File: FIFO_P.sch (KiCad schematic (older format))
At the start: 48 parts, among them J1 Vin, J3 ICLK, J4 Vout, SW1 Rotary_Encoder_61C, U1 SN74LVC2G157_MUX_TI, U10 AD7840, U2 IDT_ICS551, U3 LTC1740, U4 ARDUINO_DUE_FIFO_P_COMMANDS, U5 IDT_72V2105, U6 SN74LVC2G157_MUX_TI

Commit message: Updated missing footprints on schematic
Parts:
- C24, C32, C33, C34, C35: footprint (none) -> Capacitor_THT:C_Rect_L4.0mm_W2.5mm_P2.50mm
- NT1: footprint (none) -> NetTie:NetTie-2_SMD_Pad2.0mm
- U1, U6: footprint (none) -> Package_SO:SSOP-8_2.95x2.8mm_P0.65mm
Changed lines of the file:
@@
 F 0 "C32" H 10192 4896 50  0000 L CNN
 F 1 "0u1" H 10192 4805 50  0000 L CNN
-F 2 "" H 10100 4850 50  0001 C CNN
+F 2 "Capacitor_THT:C_Rect_L4.0mm_W2.5mm_P2.50mm" H 10100 4850 50  0001 C CNN
 F 3 "~" H 10100 4850 50  0001 C CNN
 	1    10100 4850
@@
 F 0 "C33" H 10192 5096 50  0000 L CNN
 F 1 "0u1" H 10192 5005 50  0000 L CNN
-F 2 "" H 10100 5050 50  0001 C CNN
+F 2 "Capacitor_THT:C_Rect_L4.0mm_W2.5mm_P2.50mm" H 10100 5050 50  0001 C CNN
 F 3 "~" H 10100 5050 50  0001 C CNN
 	1    10100 5050
@@
 F 0 "C34" H 10492 4896 50  0000 L CNN
 F 1 "1u" H 10492 4805 50  0000 L CNN
-F 2 "" H 10400 4850 50  0001 C CNN
+F 2 "Capacitor_THT:C_Rect_L4.0mm_W2.5mm_P2.50mm" H 10400 4850 50  0001 C CNN
 F 3 "~" H 10400 4850 50  0001 C CNN
 	1    10400 4850
@@
 F 0 "C35" H 10492 5096 50  0000 L CNN
 F 1 "1u" H 10492 5005 50  0000 L CNN
-F 2 "" H 10400 5050 50  0001 C CNN
+F 2 "Capacitor_THT:C_Rect_L4.0mm_W2.5mm_P2.50mm" H 10400 5050 50  0001 C CNN
 F 3 "~" H 10400 5050 50  0001 C CNN
 	1    10400 5050
@@
 F 0 "C24" H 10192 4546 50  0000 L CNN
 F 1 "0u1" H 10192 4455 50  0000 L CNN
-F 2 "" H 10100 4500 50  0001 C CNN
+F 2 "Capacitor_THT:C_Rect_L4.0mm_W2.5mm_P2.50mm" H 10100 4500 50  0001 C CNN
 F 3 "~" H 10100 4500 50  0001 C CNN
 	1    10100 4500
@@
 F 0 "U1" H 1800 2447 60  0000 C CNN
 F 1 "SN74LVC2G157_MUX_TI" H 1800 2341 60  0000 C CNN
-F 2 "" H 1800 1750 60  0000 C CNN
+F 2 "Package_SO:SSOP-8_2.95x2.8mm_P0.65mm" H 1800 1750 60  0001 C CNN
 F 3 "" H 1800 1750 60  0000 C CNN
 	1    1800 2050
@@
 Wire Wire Line
 	1350 2200 1350 2250
-$Comp
-L FIFO_P:SN74LVC2G157_MUX_TI U6
-U 1 1 5DD36A43
-P 1800 2850
-F 0 "U6" H 1800 3247 60  0000 C CNN
-F 1 "SN74LVC2G157_MUX_TI" H 1800 3141 60  0000 C CNN
-F 2 "" H 1800 2550 60  0000 C CNN
-F 3 "" H 1800 2550 60  0000 C CNN
-	1    1800 2850
-	1    0    0    -1
-$EndComp
 $Comp
 L power:GND #PWR06
@@
 F 0 "NT1" H 6700 7631 50  0000 C CNN
 F 1 "Net-Tie_2" H 6700 7540 50  0000 C CNN
-F 2 "" H 6700 7450 50  0001 C CNN
+F 2 "NetTie:NetTie-2_SMD_Pad2.0mm" H 6700 7450 50  0001 C CNN
 F 3 "~" H 6700 7450 50  0001 C CNN
 	1    6700 7450
@@
 Text GLabel 4350 1600 0    60   Input ~ 0
 CLK_EN
+Text GLabel 4350 2250 0    60   Input ~ 0
+DAC0
 Wire Bus Line
 	6650 6200 7550 6200
@@
 Wire Bus Line
 	7550 4150 7550 6200
-Text GLabel 4350 2250 0    60   Input ~ 0
-DAC0
+$Comp
+L FIFO_P:SN74LVC2G157_MUX_TI U6
+U 1 1 5DD36A43
+P 1800 2850
+F 0 "U6" H 1800 3247 60  0000 C CNN
+F 1 "SN74LVC2G157_MUX_TI" H 1800 3141 60  0000 C CNN
+F 2 "Package_SO:SSOP-8_2.95x2.8mm_P0.65mm" H 1800 2550 60  0001 C CNN
+F 3 "" H 1800 2550 60  0000 C CNN
+	1    1800 2850
+	1    0    0    -1
+$EndComp
 $EndSCHEMATC

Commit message: More schematic cleanup: reannotate and re-do footprints
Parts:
- removed U1, U6: SN74LVC2G157_MUX_TI, Package_SO:SSOP-8_2.95x2.8mm_P0.65mm, symbol FIFO_P:SN74LVC2G157_MUX_TI
- removed U10: AD7840, Package_DIP:DIP-24_W7.62mm, symbol FIFO_P:AD7840
- removed U2: IDT_ICS551, Package_SO:SOIC-8_3.9x4.9mm_P1.27mm, symbol FIFO_P:IDT_ICS551
- removed U3: LTC1740, FIFO_P:SSOP-36_5.3mm_Pitch0.65mm, symbol FIFO_P:LTC1740
- removed U4: ARDUINO_DUE_FIFO_P_COMMANDS, Connector_PinHeader_2.54mm:PinHeader_2x18_P2.54mm_Vertical, symbol FIFO_P:ARDUINO_DUE_FIFO_P_COMMANDS
- removed U5: IDT_72V2105, FIFO_P:LQFP-64_14x14mm_P0.8mm_HandSolder, symbol FIFO_P:IDT_72V2105
- added U1: IDT_ICS551, Package_SO:SOIC-8_3.9x4.9mm_P1.27mm, symbol FIFO_P:IDT_ICS551
- added U2, U3: SN74LVC2G157_MUX_TI, Package_SO:SSOP-8_2.95x2.8mm_P0.65mm, symbol FIFO_P:SN74LVC2G157_MUX_TI
- added U4: LTC1740, FIFO_P:SSOP-36_5.3mm_Pitch0.65mm, symbol FIFO_P:LTC1740
- added U5: ARDUINO_DUE_FIFO_P_COMMANDS, FIFO_P:Arduino_Due_Shield, symbol FIFO_P:ARDUINO_DUE_FIFO_P_COMMANDS
- added U6: IDT_72V2105, FIFO_P:LQFP-64_14x14mm_P0.8mm_HandSolder, symbol FIFO_P:IDT_72V2105
- added U8: Adafruit_128x32_OLED_I2C_1306, FIFO_P:SIP_5, symbol FIFO_P:Adafruit_128x32_OLED_I2C_1306
- added U9: AD7840, Package_SO:SSOP-24_5.3x8.2mm_P0.65mm, symbol FIFO_P:AD7840
- SW1: footprint FIFO_P:Rotary_Encoder -> FIFO_P:SIP_5
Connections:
- net labels removed: OLED_RST, SCL1, SDA1
- wire segments 305 -> 310
- no-connect marks 7 -> 8
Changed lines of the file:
@@
 	7500 1950 7900 1950
-$Comp
-L FIFO_P:Rotary_Encoder_61C SW1
-U 1 1 5C522B79
-P 9600 1550
-F 0 "SW1" H 9600 1900 50  0000 C CNN
-F 1 "Rotary_Encoder_61C" H 9500 1200 50  0000 C CNN
-F 2 "FIFO_P:Rotary_Encoder" H 9600 1550 50  0001 C CNN
-F 3 "" H 9600 1550 50  0000 C CNN
-	1    9600 1550
-	1    0    0    -1
-$EndComp
 $Comp
 L Device:R R9
@@
 Wire Wire Line
 	1400 1150 1350 1150
-$Comp
-L FIFO_P:IDT_ICS551 U2
-U 1 1 5D0AF0AA
-P 1800 1200
-F 0 "U2" H 1800 1597 60  0000 C CNN
-F 1 "IDT_ICS551" H 1800 1491 60  0000 C CNN
-F 2 "Package_SO:SOIC-8_3.9x4.9mm_P1.27mm" H 1800 1200 60  0001 C CNN
-F 3 "" H 1800 1200 60  0000 C CNN
-	1    1800 1200
-	1    0    0    -1
-$EndComp
 Wire Wire Line
 	2200 1350 2200 1450
@@
 Wire Notes Line
 	8300 2200 10000 2200
-$Comp
-L FIFO_P:AD7840 U10
-U 1 1 5921D257
-P 8600 4450
-F 0 "U10" H 9100 3200 60  0000 C CNN
-F 1 "AD7840" H 9100 4600 60  0000 C CNN
-F 2 "Package_DIP:DIP-24_W7.62mm" H 8600 4450 60  0001 C CNN
-F 3 "" H 8600 4450 60  0000 C CNN
-	1    8600 4450
-	1    0    0    -1
-$EndComp
 Wire Wire Line
 	8450 4650 8600 4650
@@
 B
 Wire Wire Line
-	7150 4550 7200 4550
-Connection ~ 7150 4550
-Connection ~ 4600 4250
-$Comp
-L FIFO_P:IDT_72V2105 U5
-U 1 1 5D0ADC94
-P 5850 4800
-F 0 "U5" H 5800 4900 60  0000 L CNN
-F 1 "IDT_72V2105" H 5550 4800 60  0000 L CNN
-F 2 "FIFO_P:LQFP-64_14x14mm_P0.8mm_HandSolder" H 5850 4800 60  0001 C CNN
-F 3 "" H 5850 4800 60  0000 C CNN
-	1    5850 4800
-	1    0    0    -1
-$EndComp
-Wire Wire Line
 	6400 4300 6400 4250
 Wire Wire Line
@@
 	6550 4500 6550 4550
 Connection ~ 6550 4550
-Wire Wire Line
-	6550 4550 7150 4550
 Wire Wire Line
 	6400 4550 6400 4500
@@
 	0    -1   -1   0
 $EndComp
-Connection ~ 7150 4250
 $Comp
 L power:GND #PWR029
@@
 Wire Wire Line
 	9950 4300 9950 4350
-$Comp
-L FIFO_P:SN74LVC2G157_MUX_TI U1
-U 1 1 5DB58231
-P 1800 2050
-F 0 "U1" H 1800 2447 60  0000 C CNN
-F 1 "SN74LVC2G157_MUX_TI" H 1800 2341 60  0000 C CNN
-F 2 "Package_SO:SSOP-8_2.95x2.8mm_P0.65mm" H 1800 1750 60  0001 C CNN
-F 3 "" H 1800 1750 60  0000 C CNN
-	1    1800 2050
-	1    0    0    -1
-$EndComp
 $Comp
 L power:GND #PWR05
@@
 Wire Wire Line
 	1650 5000 1750 5000
-Connection ~ 2000 5000
 Wire Wire Line
 	1750 5000 1750 4950
@@
 Text GLabel 1050 4900 0    60   Input ~ 0
 3.3V
-$Comp
-L FIFO_P:LTC1740 U3
-U 1 1 592106E2
-P 2000 4200
-F 0 "U3" H 2650 2350 60  0000 C CNN
-F 1 "LTC1740" H 2650 4300 60  0000 C CNN
-F 2 "FIFO_P:SSOP-36_5.3mm_Pitch0.65mm" H 2600 3400 60  0001 C CNN
-F 3 "" H 2600 3400 60  0000 C CNN
-	1    2000 4200
-	1    0    0    -1
-$EndComp
 Wire Wire Line
 	3250 3750 3250 4200
-Connection ~ 3250 4600
-Connection ~ 3250 4900
 Wire Wire Line
 	2000 4800 1950 4800
@@
 	1700 4700 1750 4700
 Connection ~ 1750 4700
-$Comp
-L FIFO_P:ARDUINO_DUE_FIFO_P_COMMANDS U4
-U 1 1 5D0AD907
-P 5850 1800
-F 0 "U4" H 5950 2637 60  0000 C CNN
-F 1 "ARDUINO_DUE_FIFO_P_COMMANDS" H 5950 2531 60  0000 C CNN
-F 2 "Connector_PinHeader_2.54mm:PinHeader_2x18_P2.54mm_Vertical" H 5850 650 60  0001 C CNN
-F 3 "" H 5850 650 60  0000 C CNN
-	1    5850 1800
-	1    0    0    -1
-$EndComp
 $Comp
 L power:GND #PWR0103
@@
 Text Label 8450 4650 0    60   ~ 0
 F13
-Text GLabel 6700 1150 1    60   Input ~ 0
-OLED_RST
-Text GLabel 6800 1150 1    60   Input ~ 0
-SCL1
-Text GLabel 6900 1150 1    60   Input ~ 0
-SDA1
 Wire Wire Line
 	2200 1150 2250 1150
@@
 Text GLabel 4350 2250 0    60   Input ~ 0
 DAC0
+$Comp
+L FIFO_P:ARDUINO_DUE_FIFO_P_COMMANDS U5
+U 1 1 5D33FDD9
+P 5850 1800
+F 0 "U5" H 5875 2653 60  0000 C CNN
+F 1 "ARDUINO_DUE_FIFO_P_COMMANDS" H 5875 2547 60  0000 C CNN
+F 2 "FIFO_P:Arduino_Due_Shield" H 9050 100 60  0001 C CNN
+F 3 "" H 9050 100 60  0000 C CNN
+	1    5850 1800
+	1    0    0    -1
+$EndComp
+$Comp
+L FIFO_P:IDT_ICS551 U1
+U 1 1 5D3416AB
+P 1800 1200
+F 0 "U1" H 1800 1597 60  0000 C CNN
+F 1 "IDT_ICS551" H 1800 1491 60  0000 C CNN
+F 2 "Package_SO:SOIC-8_3.9x4.9mm_P1.27mm" H 1800 1200 60  0001 C CNN
+F 3 "" H 1800 1200 60  0000 C CNN
+	1    1800 1200
+	1    0    0    -1
+$EndComp
+$Comp
+L FIFO_P:SN74LVC2G157_MUX_TI U2
+U 1 1 5D342EF7
+P 1800 2050
+F 0 "U2" H 1800 2447 60  0000 C CNN
+F 1 "SN74LVC2G157_MUX_TI" H 1800 2341 60  0000 C CNN
+F 2 "Package_SO:SSOP-8_2.95x2.8mm_P0.65mm" H 1800 1750 60  0001 C CNN
+F 3 "" H 1800 1750 60  0000 C CNN
+	1    1800 2050
+	1    0    0    -1
+$EndComp
+$Comp
+L FIFO_P:SN74LVC2G157_MUX_TI U3
+U 1 1 5D343B55
+P 1800 2850
+F 0 "U3" H 1800 3247 60  0000 C CNN
+F 1 "SN74LVC2G157_MUX_TI" H 1800 3141 60  0000 C CNN
+F 2 "Package_SO:SSOP-8_2.95x2.8mm_P0.65mm" H 1800 2550 60  0001 C CNN
+F 3 "" H 1800 2550 60  0000 C CNN
+	1    1800 2850
+	1    0    0    -1
+$EndComp
+$Comp
+L FIFO_P:LTC1740 U4
+U 1 1 5D344A13
+P 2000 4200
+F 0 "U4" H 2625 4447 60  0000 C CNN
+F 1 "LTC1740" H 2625 4341 60  0000 C CNN
+F 2 "FIFO_P:SSOP-36_5.3mm_Pitch0.65mm" H 2600 3400 60  0001 C CNN
+F 3 "" H 2600 3400 60  0000 C CNN
+	1    2000 4200
+	1    0    0    -1
+$EndComp
+Connection ~ 3250 4900
+Connection ~ 3250 4600
+Connection ~ 2000 5000
+$Comp
+L FIFO_P:AD7840 U9
+U 1 1 5D347427
+P 8600 4450
+F 0 "U9" H 9100 4737 60  0000 C CNN
+F 1 "AD7840" H 9100 4631 60  0000 C CNN
+F 2 "Package_SO:SSOP-24_5.3x8.2mm_P0.65mm" H 8600 4450 60  0001 C CNN
+F 3 "" H 8600 4450 60  0000 C CNN
+	1    8600 4450
+	1    0    0    -1
+$EndComp
+Wire Wire Line
+	6550 4550 7150 4550
+$Comp
+L FIFO_P:IDT_72V2105 U6
+U 1 1 5D348B40
+P 5850 4800
+F 0 "U6" H 5800 4800 60  0000 L CNN
+F 1 "IDT_72V2105" H 5550 4650 60  0000 L CNN
+F 2 "FIFO_P:LQFP-64_14x14mm_P0.8mm_HandSolder" H 5850 4800 60  0001 C CNN
+F 3 "" H 5850 4800 60  0000 C CNN
+	1    5850 4800
+	1    0    0    -1
+$EndComp
+Connection ~ 4600 4250
+Connection ~ 7150 4550
+Wire Wire Line
+	7150 4550 7200 4550
+Connection ~ 7150 4250
+$Comp
+L FIFO_P:Rotary_Encoder_61C SW1
+U 1 1 5D34AD93
+P 9600 1550
+F 0 "SW1" H 9550 1900 50  0000 L CNN
+F 1 "Rotary_Encoder_61C" H 9200 1200 50  0000 L CNN
+F 2 "FIFO_P:SIP_5" H 9600 1550 50  0001 C CNN
+F 3 "" H 9600 1550 50  0000 C CNN
+	1    9600 1550
+	1    0    0    -1
+$EndComp
+$Comp
+L FIFO_P:Adafruit_128x32_OLED_I2C_1306 U8
+U 1 1 5D38A4DF
+P 6950 650
+F 0 "U8" H 7328 645 60  0000 L CNN
+F 1 "Adafruit_128x32_OLED_I2C_1306" H 7328 539 60  0000 L CNN
+F 2 "FIFO_P:SIP_5" H 6950 650 60  0001 C CNN
+F 3 "" H 6950 650 60  0001 C CNN
+	1    6950 650
+	1    0    0    -1
+$EndComp
+NoConn ~ 7100 1000
+Text GLabel 7250 1050 2    60   Input ~ 0
++5V
+Wire Wire Line
+	7250 1050 7200 1050
+Wire Wire Line
+	7200 1050 7200 1000
+$Comp
+L power:GND #PWR09
+U 1 1 5D3C9A60
+P 7000 1000
+F 0 "#PWR09" H 7000 750 50  0001 C CNN
+F 1 "GND" H 7005 827 50  0000 C CNN
+F 2 "" H 7000 1000 50  0001 C CNN
+F 3 "" H 7000 1000 50  0001 C CNN
+	1    7000 1000
+	1    0    0    -1
+$EndComp
+Wire Wire Line
+	6700 1150 6700 1000
+Wire Wire Line
+	6800 1150 6800 1000
+Wire Wire Line
+	6900 1150 6900 1000
 Wire Bus Line
 	6650 6200 7550 6200
@@
 Wire Bus Line
 	7550 4150 7550 6200
-$Comp
-L FIFO_P:SN74LVC2G157_MUX_TI U6
-U 1 1 5DD36A43
-P 1800 2850
-F 0 "U6" H 1800 3247 60  0000 C CNN
-F 1 "SN74LVC2G157_MUX_TI" H 1800 3141 60  0000 C CNN
-F 2 "Package_SO:SSOP-8_2.95x2.8mm_P0.65mm" H 1800 2550 60  0001 C CNN
-F 3 "" H 1800 2550 60  0000 C CNN
-	1    1800 2850
-	1    0    0    -1
-$EndComp
 $EndSCHEMATC

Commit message: Added screw terminal; put some new IC footprints in place
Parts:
- added SW1: HIST_PROG, Button_Switch_THT:SW_PUSH_6mm_H13mm, symbol Switch:SW_SPST
- NT1: footprint NetTie:NetTie-2_SMD_Pad2.0mm -> NetTie:NetTie-2_THT_Pad1.0mm
- SW2: renamed from SW1; footprint FIFO_P:SIP_5 -> Connector_PinHeader_2.54mm:PinHeader_1x06_P2.54mm_Vertical
- U7: renamed from U8; footprint FIFO_P:SIP_5 -> Connector_PinHeader_2.54mm:PinHeader_1x06_P2.54mm_Vertical
- renumbered C7 to C1, C23 to C10, C10 to C11, C11 to C12, C12 to C13, C13 to C14, C14 to C15, C15 to C16, C16 to C17, C17 to C18, C18 to C19, C1 to C2, C19 to C20, C24 to C21, C32 to C22, C33 to C23, C34 to C24, C35 to C25, C2 to C3, C3 to C4, C6 to C5, C4 to C6, C5 to C7, C9 to C8, C8 to C9, J3 to J2, J4 to J3, R5 to R2, R6 to R3, R7 to R4, R9 to R5, R8 to R6, U9 to U8
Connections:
- wire segments 310 -> 318
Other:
- moved on the sheet: U7

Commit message: More progress on final board
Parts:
- C1, C10, C11, C12, C13, C15, C17, C19, C2, C21, C22, C23, C24, C25, C3, C4, C5, C6, C7, C8, C9: footprint Capacitor_THT:C_Rect_L4.0mm_W2.5mm_P2.50mm -> Capacitor_SMD:C_0805_2012Metric_Pad1.15x1.40mm_HandSolder
- C14, C16, C18, C20: footprint Capacitor_THT:C_Disc_D5.0mm_W2.5mm_P2.50mm -> Capacitor_SMD:C_0805_2012Metric_Pad1.15x1.40mm_HandSolder
- U5: footprint FIFO_P:Arduino_Due_Shield -> FIFO_P:Arduino_Due_Selected_Pins
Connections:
- wire segments 318 -> 319

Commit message: Reannotated and replaced many components. Bypass capacitors everywhere.
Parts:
- removed NT1: Net-Tie_2, NetTie:NetTie-2_THT_Pad1.0mm, symbol Device:Net-Tie_2
- added C14, C15, C22, C23, C37, C38, C4, C5: 10u, Capacitor_SMD:C_0805_2012Metric_Pad1.15x1.40mm_HandSolder, symbol Device:C
- added C16, C20, C30, C36, C7: 1u, Capacitor_SMD:C_0805_2012Metric_Pad1.15x1.40mm_HandSolder, symbol Device:C
- added J3: Screw_Terminal_01x08, TerminalBlock_Phoenix:TerminalBlock_Phoenix_MKDS-3-8-5.08_1x08_P5.08mm_Horizontal, symbol Connector:Screw_Terminal_01x08
- added J4: Jack-DC, Connector_BarrelJack:BarrelJack_Horizontal, symbol Connector:Jack-DC
- added TP1, TP3, TP5, TP7: TestPoint, FIFO_P:Test_Pin, symbol Connector:TestPoint
- added U11: LM2776, Package_TO_SOT_SMD:SOT-23-6, symbol Regulator_SwitchedCapacitor:LM2776
- added U5: LM2940CT-5.0, Package_TO_SOT_THT:TO-220-3_Horizontal_TabDown, symbol FIFO_P:LM2940CT-5.0
- added U6: LM1117-3.3, Package_TO_SOT_SMD:TO-252-3_TabPin2, symbol Regulator_Linear:LM1117-3.3
- renumbered C7 to C10, C8 to C11, C9 to C12, C10 to C13, C11 to C17, C12 to C18, C13 to C19, C14 to C21, C15 to C24, C16 to C25, C17 to C26, C18 to C27, C19 to C28, C20 to C29, C21 to C31, C22 to C32, C23 to C33, C24 to C34, C25 to C35, C4 to C6, C5 to C8, C6 to C9, J3 to J5, TP1 to TP2, TP2 to TP4, TP3 to TP6, U8 to U10, U5 to U7, U6 to U8, U7 to U9
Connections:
- net labels added: V+
- wire segments 319 -> 407
- no-connect marks 8 -> 11
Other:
- note added: "5V and 3.3V Regulation"
- note added: "Charge Pump Inverter for -5V"
- note added: "Clock Distribution and Control"
- note removed: "Clock distribution and control"
- moved on the sheet: C1, C17, C18, C2, C3, C31, C32, C33, C34, C35, C6, D1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

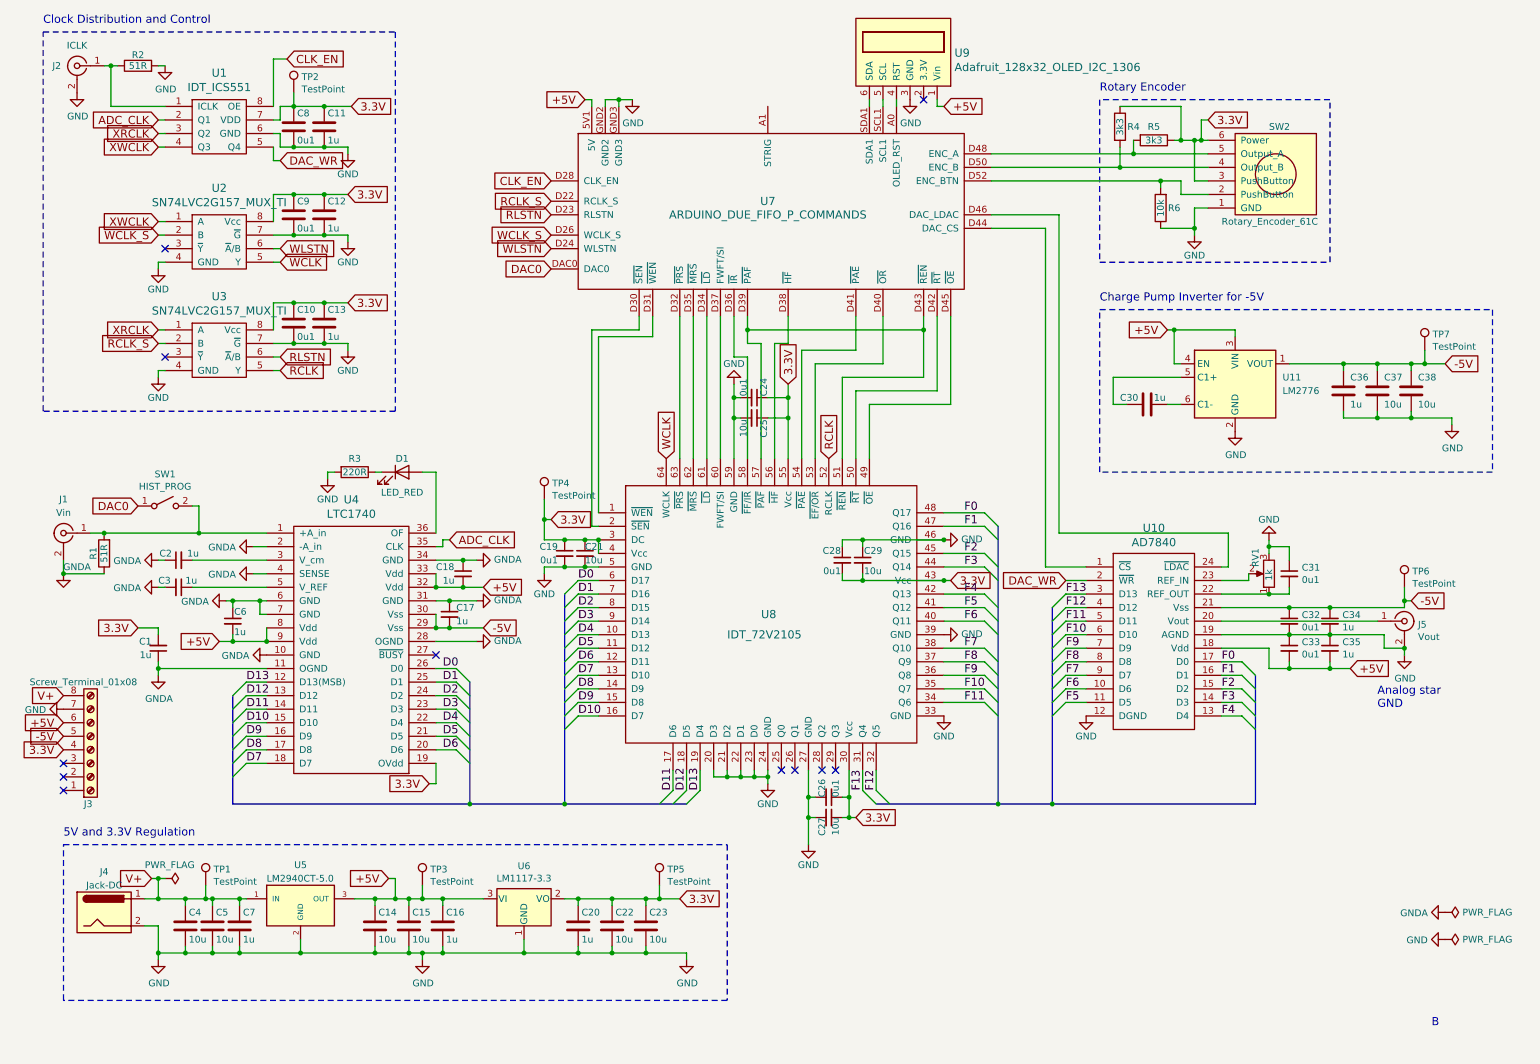
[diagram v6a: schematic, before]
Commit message: More work. TODO: Change muxes to clock ADC and both R/WCLKs, not RCLK and WCLK
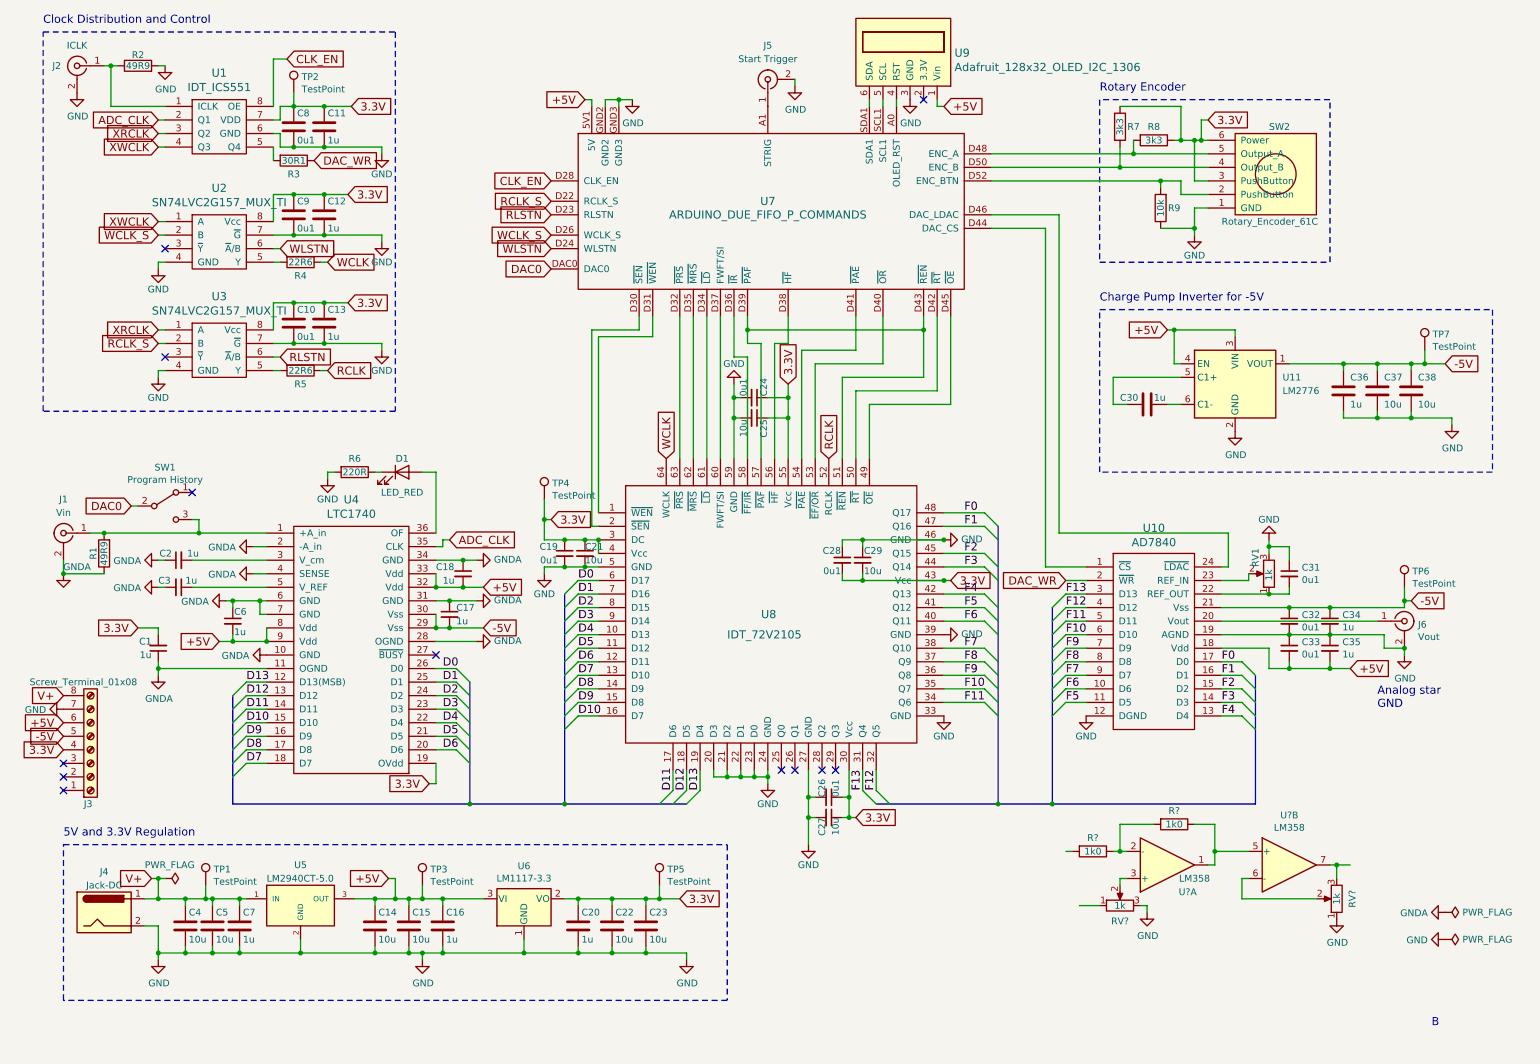
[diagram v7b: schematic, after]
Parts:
- removed SW1: HIST_PROG, Button_Switch_THT:SW_PUSH_6mm_H13mm, symbol Switch:SW_SPST
- added J5: Start Trigger, Connector_Coaxial:BNC_TEConnectivity_1478204_Vertical, symbol Connector:Conn_Coaxial
- added R3: 30R1, Resistor_SMD:R_0805_2012Metric_Pad1.15x1.40mm_HandSolder, symbol Device:R
- added R4, R5: 22R6, Resistor_SMD:R_0805_2012Metric_Pad1.15x1.40mm_HandSolder, symbol Device:R
- added R? (x2): 1k0, symbol Device:R
- added RV? (x2): 1k, symbol Device:R_POT
- added SW1: Program History, Button_Switch_THT:SW_Slide_1P2T_CK_OS102011MS2Q, symbol Switch:SW_SPDT
- added U? (x2): LM358, symbol Amplifier_Operational:LM358
- R1, R2: value 51R -> 49R9; footprint Resistor_THT:R_Axial_DIN0204_L3.6mm_D1.6mm_P7.62mm_Horizontal -> Resistor_SMD:R_0805_2012Metric_Pad1.15x1.40mm_HandSolder
- renumbered J5 to J6, R3 to R6, R4 to R7, R5 to R8, R6 to R9
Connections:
- net DAC0: now also SW1.2 (B)
- net DAC_WR: now also R3.1; no longer U1.5 (Q4)
- net GND: now also J5.2 (Ext), RV?.1, RV?.3
- net RCLK: now also R5.1; no longer U3.5 (Y)
- net WCLK: now also R4.1; no longer U2.5 (Y)
- net at J1.1 (In), R1.2, U4.1 (+A_in): now also SW1.3 (C)
- net at U7.A1 (STRIG): now also J5.1 (In)
- new net: R3.2, U1.5 (Q4)
- new net: R4.2, U2.5 (Y)
- new net: R5.2, U3.5 (Y)
- new net: R?.1, U?.1, U?.5 (+)
- new net: R?.1, R?.2, U?.2 (-)
- new net: RV?.2, U?.3 (+)
- new net: RV?.2, U?.6 (-)
- new net: RV?.3, U?.7
- no-connect marks 11 -> 12
